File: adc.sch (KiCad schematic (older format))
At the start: 19 parts

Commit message: updates to gp_dac
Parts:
- gave numbers to parts that had none: 19
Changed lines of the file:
@@
 $Descr A 11000 8500
 encoding utf-8
-Sheet 7 9
+Sheet 7 10
 Title ""
 Date ""
@@
 $EndDescr
 $Comp
-L Device:C C?
+L Device:C C24
 U 1 1 B0DC2316
 P 7050 3700
-F 0 "C?" H 7090 3725 59  0000 L BNN
+F 0 "C24" H 7090 3725 59  0000 L BNN
 F 1 "100p" H 7090 3535 59  0000 L BNN
 F 2 "Capacitor_SMD:C_0603_1608Metric" H 7050 3700 50  0001 C CNN
@@
 $EndComp
 $Comp
-L Device:R_US R?
+L Device:R_US R31
 U 1 1 B996151F
 P 2450 4600
-F 0 "R?" H 2300 4659 59  0000 L BNN
+F 0 "R31" H 2300 4659 59  0000 L BNN
 F 1 "100" H 2300 4470 59  0000 L BNN
 F 2 "Resistor_SMD:R_0603_1608Metric" H 2450 4600 50  0001 C CNN
@@
 $EndComp
 $Comp
-L Device:C C?
+L Device:C C18
 U 1 1 56DFCCD0
 P 5350 2750
-F 0 "C?" H 5390 2775 59  0000 L BNN
+F 0 "C18" H 5390 2775 59  0000 L BNN
 F 1 "0.1u" H 5390 2585 59  0000 L BNN
 F 2 "Capacitor_SMD:C_0603_1608Metric" H 5350 2750 50  0001 C CNN
@@
 $EndComp
 $Comp
-L Device:R_US R?
+L Device:R_US R32
 U 1 1 BF33D434
 P 4650 4700
-F 0 "R?" H 4500 4759 59  0000 L BNN
+F 0 "R32" H 4500 4759 59  0000 L BNN
 F 1 "100" H 4500 4570 59  0000 L BNN
 F 2 "Resistor_SMD:R_0603_1608Metric" H 4650 4700 50  0001 C CNN
@@
 $EndComp
 $Comp
-L Device:C C?
+L Device:C C19
 U 1 1 C9238E33
 P 5400 4300
-F 0 "C?" H 5440 4325 59  0000 L BNN
+F 0 "C19" H 5440 4325 59  0000 L BNN
 F 1 "0.1u" H 5440 4135 59  0000 L BNN
 F 2 "Capacitor_SMD:C_0603_1608Metric" H 5400 4300 50  0001 C CNN
@@
 $EndComp
 $Comp
-L Device:C C?
+L Device:C C20
 U 1 1 E612D2BB
 P 5800 4300
-F 0 "C?" H 5840 4325 59  0000 L BNN
+F 0 "C20" H 5840 4325 59  0000 L BNN
 F 1 "0.1u" H 5840 4135 59  0000 L BNN
 F 2 "Capacitor_SMD:C_0603_1608Metric" H 5800 4300 50  0001 C CNN
@@
 $EndComp
 $Comp
-L Device:C C?
+L Device:C C13
 U 1 1 1FADEAAB
 P 1450 3400
-F 0 "C?" H 1490 3425 59  0000 L BNN
+F 0 "C13" H 1490 3425 59  0000 L BNN
 F 1 "0.1u" H 1490 3235 59  0000 L BNN
 F 2 "Capacitor_SMD:C_0603_1608Metric" H 1450 3400 50  0001 C CNN
@@
 $EndComp
 $Comp
-L Device:C C?
+L Device:C C15
 U 1 1 9D5B9004
 P 1850 3400
-F 0 "C?" H 1890 3425 59  0000 L BNN
+F 0 "C15" H 1890 3425 59  0000 L BNN
 F 1 "0.1u" H 1890 3235 59  0000 L BNN
 F 2 "Capacitor_SMD:C_0603_1608Metric" H 1850 3400 50  0001 C CNN
@@
 $EndComp
 $Comp
-L Device:R_US R?
+L Device:R_US R33
 U 1 1 87DF8B8E
 P 7650 3400
-F 0 "R?" H 7500 3459 59  0000 L BNN
+F 0 "R33" H 7500 3459 59  0000 L BNN
 F 1 "33" H 7500 3270 59  0000 L BNN
 F 2 "Resistor_SMD:R_0603_1608Metric" H 7650 3400 50  0001 C CNN
@@
 $EndComp
 $Comp
-L Device:R_US R?
+L Device:R_US R34
 U 1 1 BFC3FA38
 P 7650 4150
-F 0 "R?" H 7500 4209 59  0000 L BNN
+F 0 "R34" H 7500 4209 59  0000 L BNN
 F 1 "33" H 7500 4020 59  0000 L BNN
 F 2 "Resistor_SMD:R_0603_1608Metric" H 7650 4150 50  0001 C CNN
@@
 $EndComp
 $Comp
-L Device:C C?
+L Device:C C17
 U 1 1 E8572435
 P 3450 5800
-F 0 "C?" H 3150 5800 59  0000 L BNN
+F 0 "C17" H 3150 5800 59  0000 L BNN
 F 1 "0.1u" H 3200 5650 59  0000 L BNN
 F 2 "Capacitor_SMD:C_0603_1608Metric" H 3450 5800 50  0001 C CNN
@@
 $EndComp
 $Comp
-L adc_dac_v1-eagle-import:AD7960BCPZ-RL7 U?
+L adc_dac_v1-eagle-import:AD7960BCPZ-RL7 U22
 U 1 1 70C280EF
 P 3550 3800
-F 0 "U?" H 4264 4859 69  0000 L BNN
+F 0 "U22" H 4264 4859 69  0000 L BNN
 F 1 "AD7960BCPZ-RL7" H 4239 4659 69  0000 L BNN
 F 2 "adc_dac_v1:CP_32_7" H 3550 3800 50  0001 C CNN
@@
 $EndComp
 $Comp
-L Device:C C?
+L Device:C C16
 U 1 1 32508C8E
 P 2450 2850
-F 0 "C?" H 2490 2875 59  0000 L BNN
+F 0 "C16" H 2490 2875 59  0000 L BNN
 F 1 "10u" H 2490 2685 59  0000 L BNN
 F 2 "Capacitor_SMD:C_0603_1608Metric" H 2450 2850 50  0001 C CNN
@@
 $EndComp
 $Comp
-L adc_dac_v1-eagle-import:PINHD-1X04_2.54-SMD JP?
+L adc_dac_v1-eagle-import:PINHD-1X04_2.54-SMD JP1
 U 1 1 93E45719
 P 9100 3800
-F 0 "JP?" H 8850 4125 59  0000 L BNN
+F 0 "JP1" H 8850 4125 59  0000 L BNN
 F 1 "PINHD-1X04_2.54-SMD" H 8850 3500 59  0000 L BNN
 F 2 "adc_dac_v1:1X04SMD" H 9100 3800 50  0001 C CNN
@@
 5.1 kOhm output impedance\nMust buffer\n
 $Comp
-L covg-kicad:OPA325 U?
+L covg-kicad:OPA325 U23
 U 1 1 60CEDBBA
 P 7650 4850
-F 0 "U?" H 7994 4896 50  0000 L CNN
+F 0 "U23" H 7994 4896 50  0000 L CNN
 F 1 "OPA325" H 7994 4805 50  0000 L CNN
 F 2 "Package_TO_SOT_SMD:SOT-23-5" H 7550 4650 50  0001 L CNN
@@
 Connection ~ 8000 4850
 $Comp
-L Device:R_US R?
+L Device:R_US R35
 U 1 1 60D076A5
 P 8500 4850
-F 0 "R?" H 8350 4909 59  0000 L BNN
+F 0 "R35" H 8350 4909 59  0000 L BNN
 F 1 "33" H 8350 4720 59  0000 L BNN
 F 2 "Resistor_SMD:R_0603_1608Metric" H 8500 4850 50  0001 C CNN
@@
 	8650 4850 9300 4850
 $Comp
-L Device:C C?
+L Device:C C27
 U 1 1 60D0F62A
 P 8350 5550
-F 0 "C?" H 8390 5575 59  0000 L BNN
+F 0 "C27" H 8390 5575 59  0000 L BNN
 F 1 "0.1u" H 8390 5385 59  0000 L BNN
 F 2 "Capacitor_SMD:C_0603_1608Metric" H 8350 5550 50  0001 C CNN
@@
 	2450 3000 2450 3200
 $Comp
-L Device:C C?
+L Device:C C14
 U 1 1 60D49EBB
 P 1450 4000
-F 0 "C?" H 1490 4025 59  0000 L BNN
+F 0 "C14" H 1490 4025 59  0000 L BNN
 F 1 "0.1u" H 1200 3850 59  0000 L BNN
 F 2 "Capacitor_SMD:C_0603_1608Metric" H 1450 4000 50  0001 C CNN
@@
 	1450 3800 1350 3800
 $Comp
-L Device:C C?
+L Device:C C23
 U 1 1 60D51F18
 P 6100 4950
-F 0 "C?" H 6140 4975 59  0000 L BNN
+F 0 "C23" H 6140 4975 59  0000 L BNN
 F 1 "0.1u" H 6140 4785 59  0000 L BNN
 F 2 "Capacitor_SMD:C_0603_1608Metric" H 6100 4950 50  0001 C CNN

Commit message: completed gp adc
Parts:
- removed JP1: PINHD-1X04_2.54-SMD, adc_dac_v1:1X04SMD, symbol adc_dac_v1-eagle-import:PINHD-1X04_2.54-SMD
- added J?: Conn_01x04_Male, symbol Connector:Conn_01x04_Male
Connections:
- wire segments 119 -> 120
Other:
- note added: "Use internal buffer (x2) with 2.048V ref. \n “External reference of 2.048 V applied to the REFIN pin\n(high impedance input). The on-chip buffer gains this by 2\nand drives the REF pin with 4.096 V” \nEN3=X, EN2=0, EN1=0, EN0=1 (28 MHz BW)\nEN3=X, EN2=1, EN1=0, EN0=1 (9 MHz BW, use this BW only when the throughput is 2 MSPS or lower)"
- note removed: "Use internal buffer (x2) with 2.048V ref. \n “External reference of 2.048 V applied to the REFIN pin\n(high impedance input). The on-chip buffer gains this by 2\nand drives the REF pin with 4.096 V” \nEN3=X, EN2=0, EN1=0, EN0=1 (28 MHz BW)\nEN3=X, EN2=1, EN1=0, EN0=1 (9 MHz BW)"
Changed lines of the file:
@@
 	1    0    0    -1
-$EndComp
-$Comp
-L adc_dac_v1-eagle-import:PINHD-1X04_2.54-SMD JP1
-U 1 1 93E45719
-P 9100 3800
-F 0 "JP1" H 8850 4125 59  0000 L BNN
-F 1 "PINHD-1X04_2.54-SMD" H 8850 3500 59  0000 L BNN
-F 2 "adc_dac_v1:1X04SMD" H 9100 3800 50  0001 C CNN
-F 3 "" H 9100 3800 50  0001 C CNN
-	1    9100 3800
-	-1   0    0    -1
 $EndComp
 Text Label 5050 4000 0    70   ~ 0
@@
 IN_P_LP
 Text Notes 650  1200 0    59   ~ 0
-Use internal buffer (x2) with 2.048V ref.  \n “External reference of 2.048 V applied to the REFIN pin\n(high impedance input). The on-chip buffer gains this by 2\nand drives the REF pin with 4.096 V” \nEN3=X, EN2=0, EN1=0, EN0=1 (28 MHz BW)\nEN3=X, EN2=1, EN1=0, EN0=1 (9 MHz BW)
+Use internal buffer (x2) with 2.048V ref.  \n “External reference of 2.048 V applied to the REFIN pin\n(high impedance input). The on-chip buffer gains this by 2\nand drives the REF pin with 4.096 V” \nEN3=X, EN2=0, EN1=0, EN0=1 (28 MHz BW)\nEN3=X, EN2=1, EN1=0, EN0=1 (9 MHz BW, use this BW only when the throughput is 2 MSPS or lower)
 Text Notes 650  1450 0    59   ~ 0
 VDD2 and VIO can come from the same supply. \nBut route and decouple separately.
-Text Notes 9000 3800 2    59   ~ 0
+Text Notes 8900 3800 2    59   ~ 0
 Alternative signal connection\nor ground the inputs
 Wire Wire Line
@@
 L power:+1V8 #PWR0104
 U 1 1 61635B4D
-P 3850 2500
-F 0 "#PWR0104" H 3850 2350 50  0001 C CNN
-F 1 "+1V8" H 3865 2673 50  0000 C CNN
-F 2 "" H 3850 2500 50  0001 C CNN
-F 3 "" H 3850 2500 50  0001 C CNN
-	1    3850 2500
-	1    0    0    -1
-$EndComp
-Connection ~ 3850 2500
+P 3850 2400
+F 0 "#PWR0104" H 3850 2250 50  0001 C CNN
+F 1 "+1V8" H 3865 2573 50  0000 C CNN
+F 2 "" H 3850 2400 50  0001 C CNN
+F 3 "" H 3850 2400 50  0001 C CNN
+	1    3850 2400
+	1    0    0    -1
+$EndComp
 $Comp
 L power:+1V8 #PWR0105
@@
 Text HLabel 2250 3900 0    50   Input ~ 0
 A_EN0
+$Comp
+L Connector:Conn_01x04_Male J?
+U 1 1 628E78F9
+P 9000 3700
+F 0 "J?" H 9108 3981 50  0000 C CNN
+F 1 "Conn_01x04_Male" H 9108 3890 50  0000 C CNN
+F 2 "" H 9000 3700 50  0001 C CNN
+F 3 "~" H 9000 3700 50  0001 C CNN
+	1    9000 3700
+	1    0    0    -1
+$EndComp
+Wire Wire Line
+	3850 2400 3850 2500
+Connection ~ 3850 2500
 $EndSCHEMATC

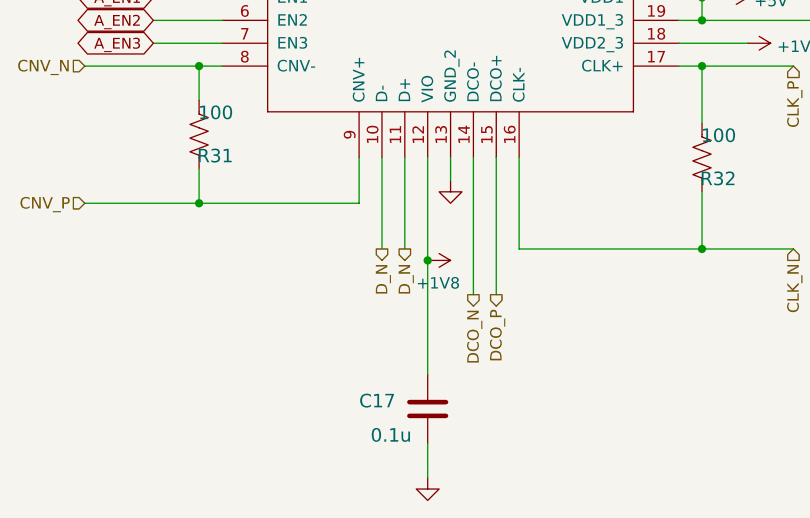
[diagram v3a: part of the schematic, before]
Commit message: modify LVDS connections for AD7960
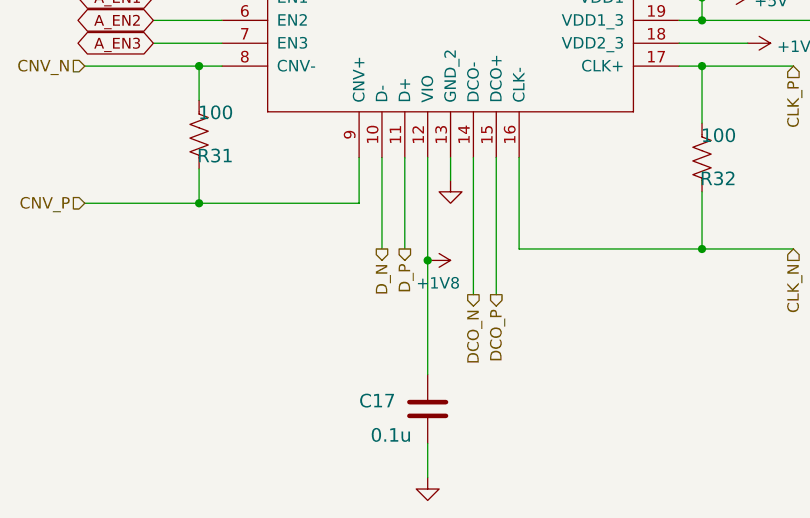
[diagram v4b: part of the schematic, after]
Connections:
- net D_N: no longer U22.11 (D+)
- new net D_P: U22.11 (D+)
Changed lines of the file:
@@
 D_N
 Text HLabel 3350 5100 3    50   Output ~ 0
-D_N
+D_P
 Text HLabel 3650 5300 3    50   Output ~ 0
 DCO_N

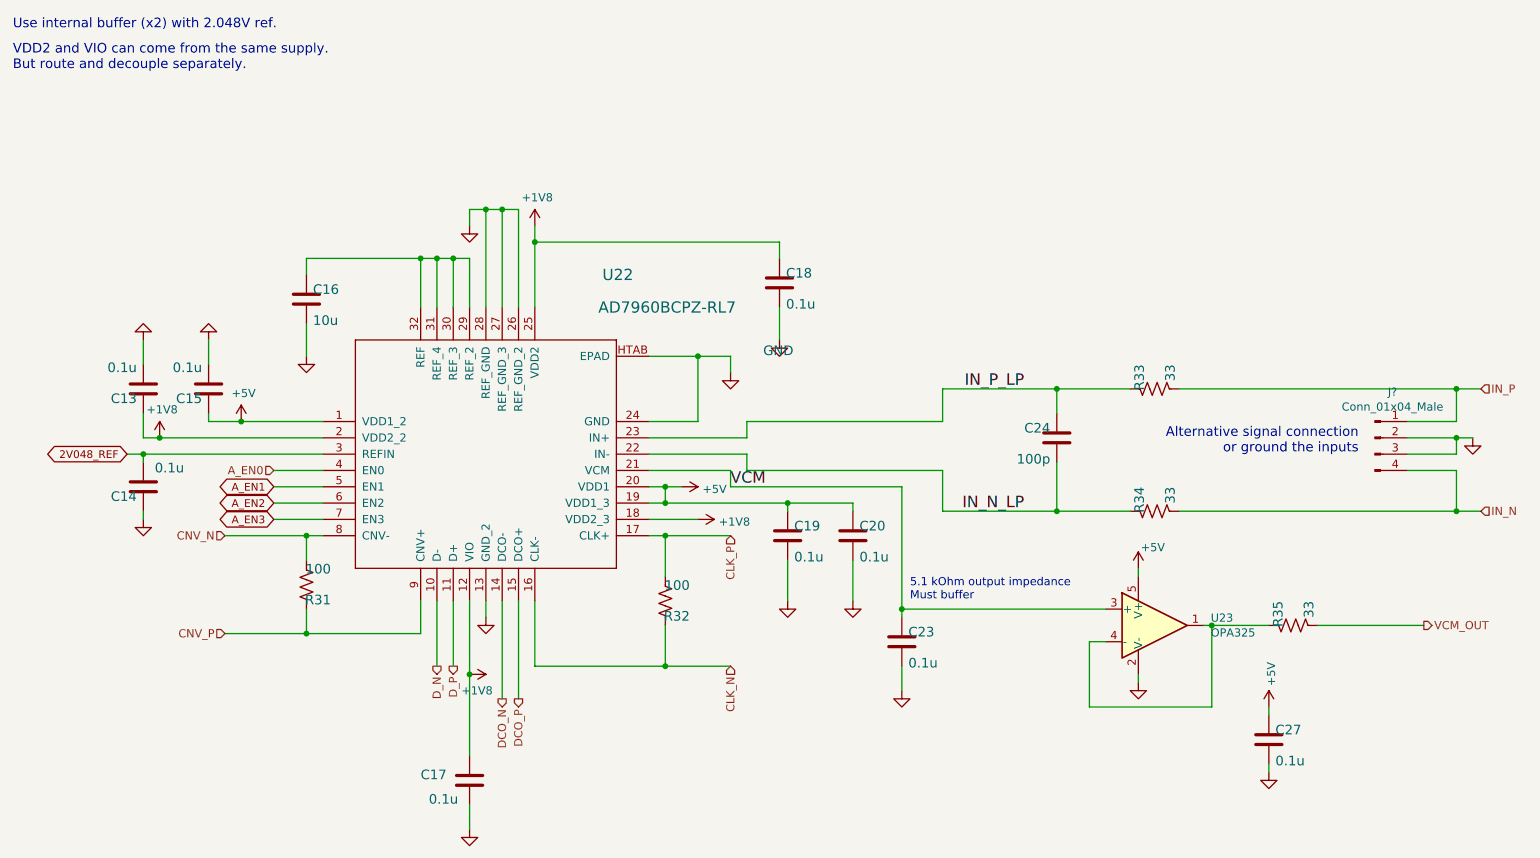
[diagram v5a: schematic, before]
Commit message: corrected most ERC errors
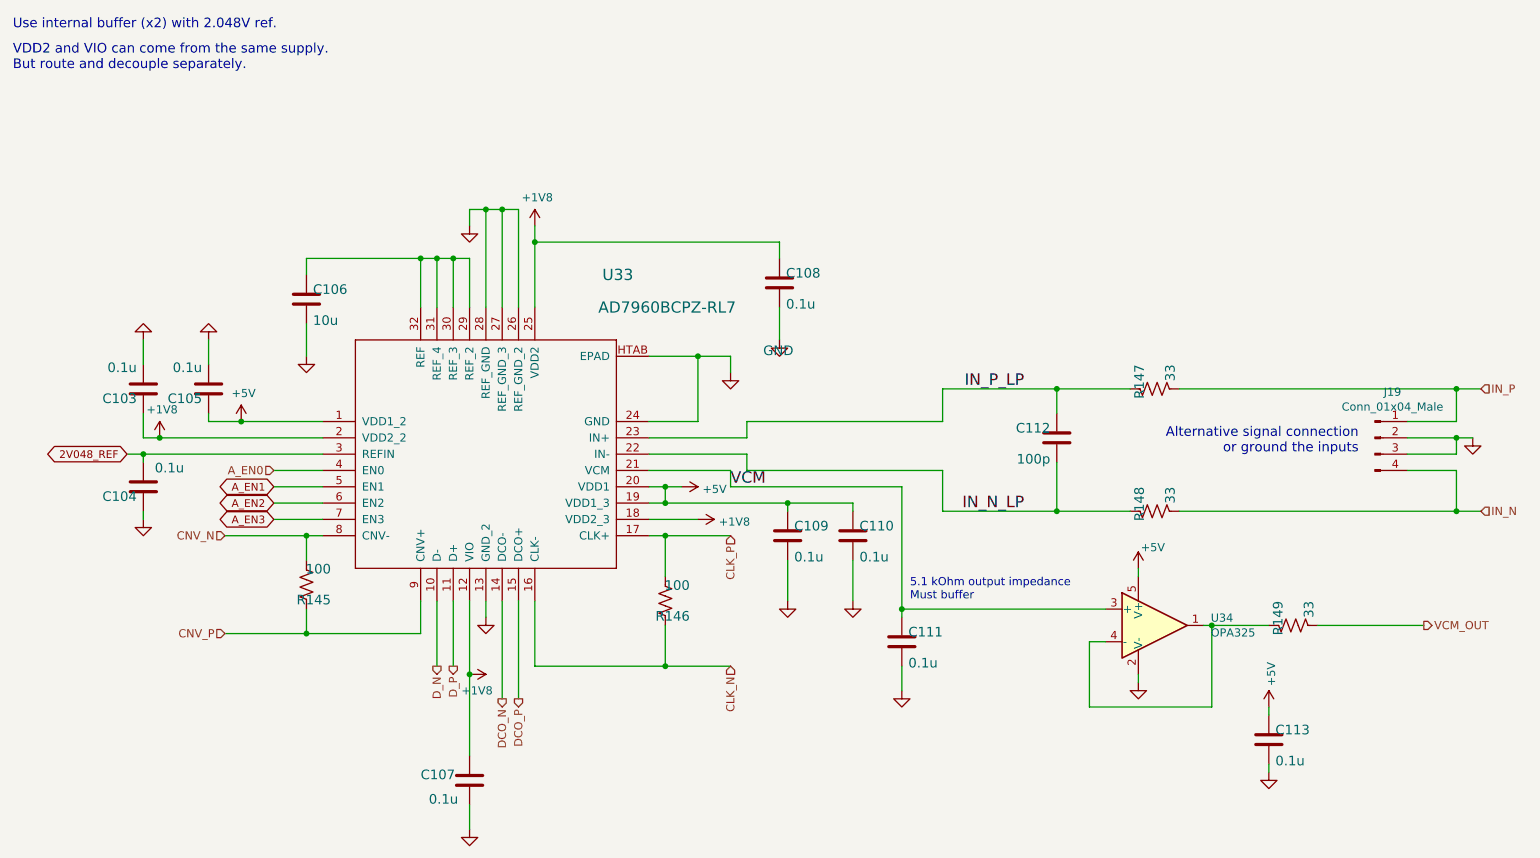
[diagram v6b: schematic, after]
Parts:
- gave numbers to parts that had none: 1

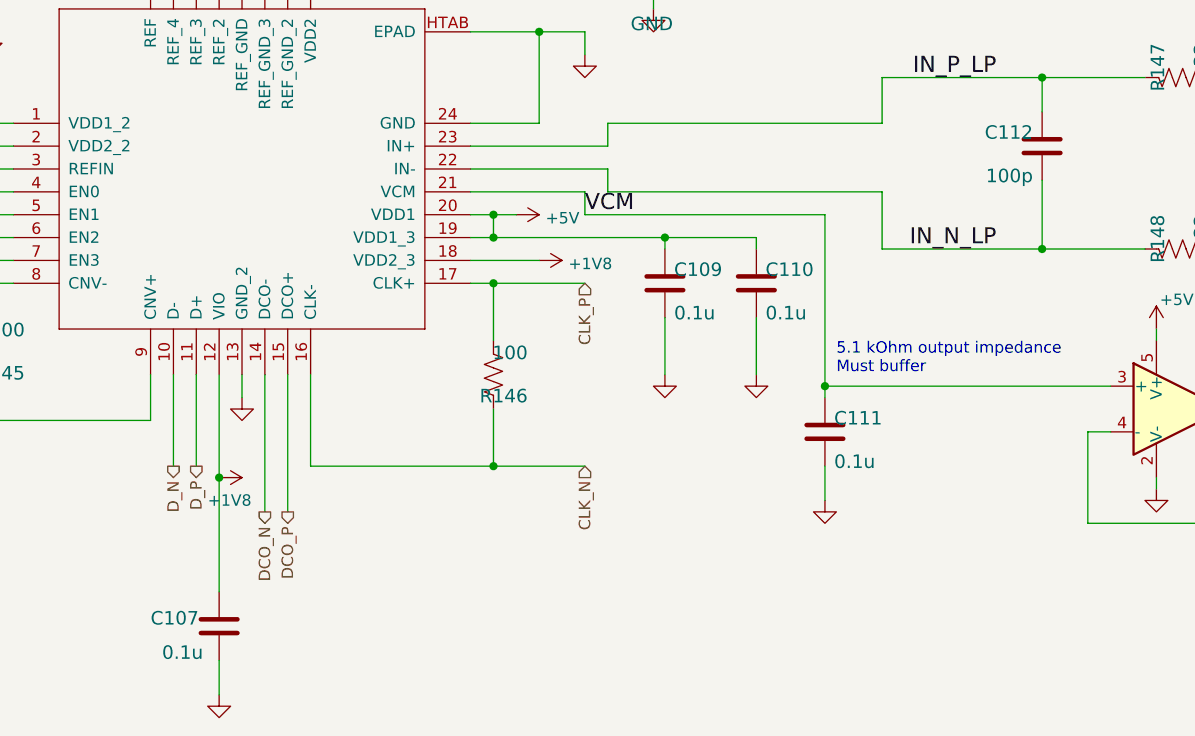
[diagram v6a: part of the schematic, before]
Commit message: after using kifield to update Manf#
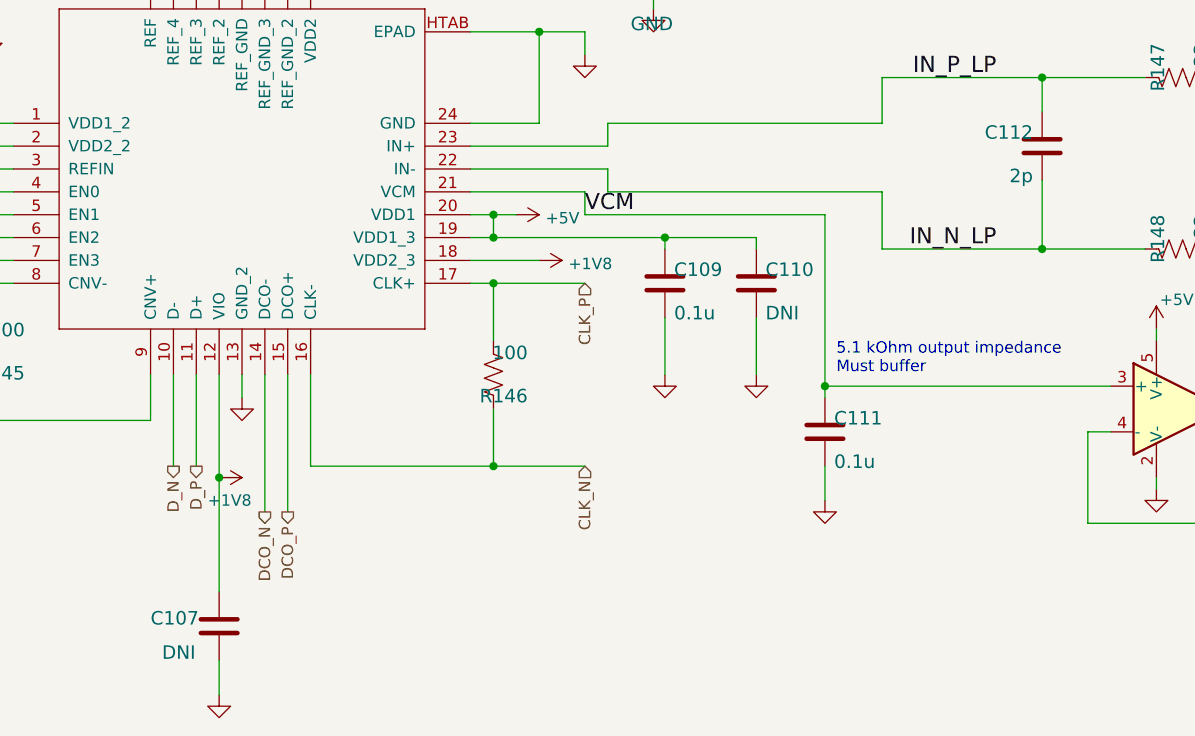
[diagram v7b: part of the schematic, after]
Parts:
- C13, C14, C15, C18, C19, C23, C27: Manf# (none) -> CC0603MRX7R8BB104; Manufacturer_Name (none) -> Yageo; Tolerance (none) -> 20%; voltage (none) -> 25
- C16: Manf# (none) -> JMK107ABJ106KAHT; Tolerance (none) -> 10%; voltage (none) -> 6.3V
- C17, C20: value 0.1u -> DNI
- C24: value 100p -> 2p; Manf# (none) -> CC0603CRNPO9BN2R0; Tolerance (none) -> 0.25pF; voltage (none) -> 50V
- R31, R32: Manf# (none) -> RC0603FR-07100RL; Power (none) -> 0.1W; Tolerance (none) -> 1%
- R33, R34, R35: Manf# (none) -> RC0603FR-0733RL; Power (none) -> 0.1W; Tolerance (none) -> 1%
- U22: Manf# (none) -> AD7961BCPZ-RL7
- U23: Manf# (none) -> OPA325IDBVR
